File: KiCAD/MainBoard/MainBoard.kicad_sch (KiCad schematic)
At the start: 84 parts, among them J1 DB25, J2 Raspberry_Pi_2_3, P1 CONN_02X04, P10 CONN_01X03, P11 CONN_01X03, P12 CONN_01X03, P13 CONN_01X03, P14 CONN_01X02, P15 CONN_02X07, P16 CONN_02X04, P18 CONN_01X03, P2 CONN_01X04, P3 CONN_02X04, P4 HOLE, P5 HOLE, P6 HOLE, P7 HOLE, P8 CONN_01X02, P9 CONN_01X03, Q1 BSS138, Q2 BSS138, Q3 DMN65D8L, U1 mp2307, U10 SI4425DDY, U11 INA199A2, U12 ADS1015, U13 DYS_mini_ESC, U14 DYS_mini_ESC, U15 DYS_mini_ESC, U2 DYS_mini_ESC, U3 DYS_mini_ESC, U4 DYS_mini_ESC, U5 DYS_mini_ESC, U6 TLV1117LV33, U7 TENDA_P200, U8 pca9685, U9 DYS_mini_ESC

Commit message: moved BLDC to seperate sheet
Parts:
- removed C13, C14, C15, C16, C6, C7, C8, C9: 220uF/25V, Capacitor_SMD:CP_Elec_8x10, symbol Device:C_Polarized_Small
- removed P3: CONN_02X04, Socket_Strips:Socket_Strip_Straight_2x04, symbol MainBoard-rescue:CONN_02X04
- removed U13, U14, U15, U2, U3, U4, U5, U9: DYS_mini_ESC, footprint:DYS_Mini_ESC, symbol custom_lib:DYS_mini_ESC
- P1: value CONN_02X04 -> BDLC Enable; footprint Socket_Strips:Socket_Strip_Straight_2x04 -> Connector_PinSocket_2.54mm:PinSocket_2x08_P2.54mm_Vertical; symbol MainBoard-rescue:CONN_02X04 -> Connector_Generic:Conn_02x08_Odd_Even
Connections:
- net CH10: now also P1.2 (Pin_2)
- net CH11: now also P1.4 (Pin_4)
- net CH12: now also P1.10 (Pin_10); no longer P1.2 (P2)
- net CH13: now also P1.12 (Pin_12); no longer P1.4 (P4)
- net CH14: now also P1.14 (Pin_14); no longer P1.6 (P6)
- net CH15: now also P1.16 (Pin_16); no longer P1.8 (P8)
- net CH6: now also P1.8 (Pin_8)
- net CH7: now also P1.6 (Pin_6)
- net ESC5 renamed Brushless DC Controllers/ESC1
- net ESC6 renamed Brushless DC Controllers/ESC2
- net ESC7 renamed Brushless DC Controllers/ESC3
- net ESC8 renamed Brushless DC Controllers/ESC4
- new net Brushless DC Controllers/ESC5: P1.9 (Pin_9)
- new net Brushless DC Controllers/ESC6: P1.11 (Pin_11)
- new net Brushless DC Controllers/ESC7: P1.13 (Pin_13)
- new net Brushless DC Controllers/ESC8: P1.15 (Pin_15)
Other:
- added sheet Brushless DC Controllers (BLDC.kicad_sch)
- note removed: "BLDC ESC X 8"
- moved on the sheet: C21, D1, D2, P14, Q3, R15, R16, R17, R6, R7, U10, U7

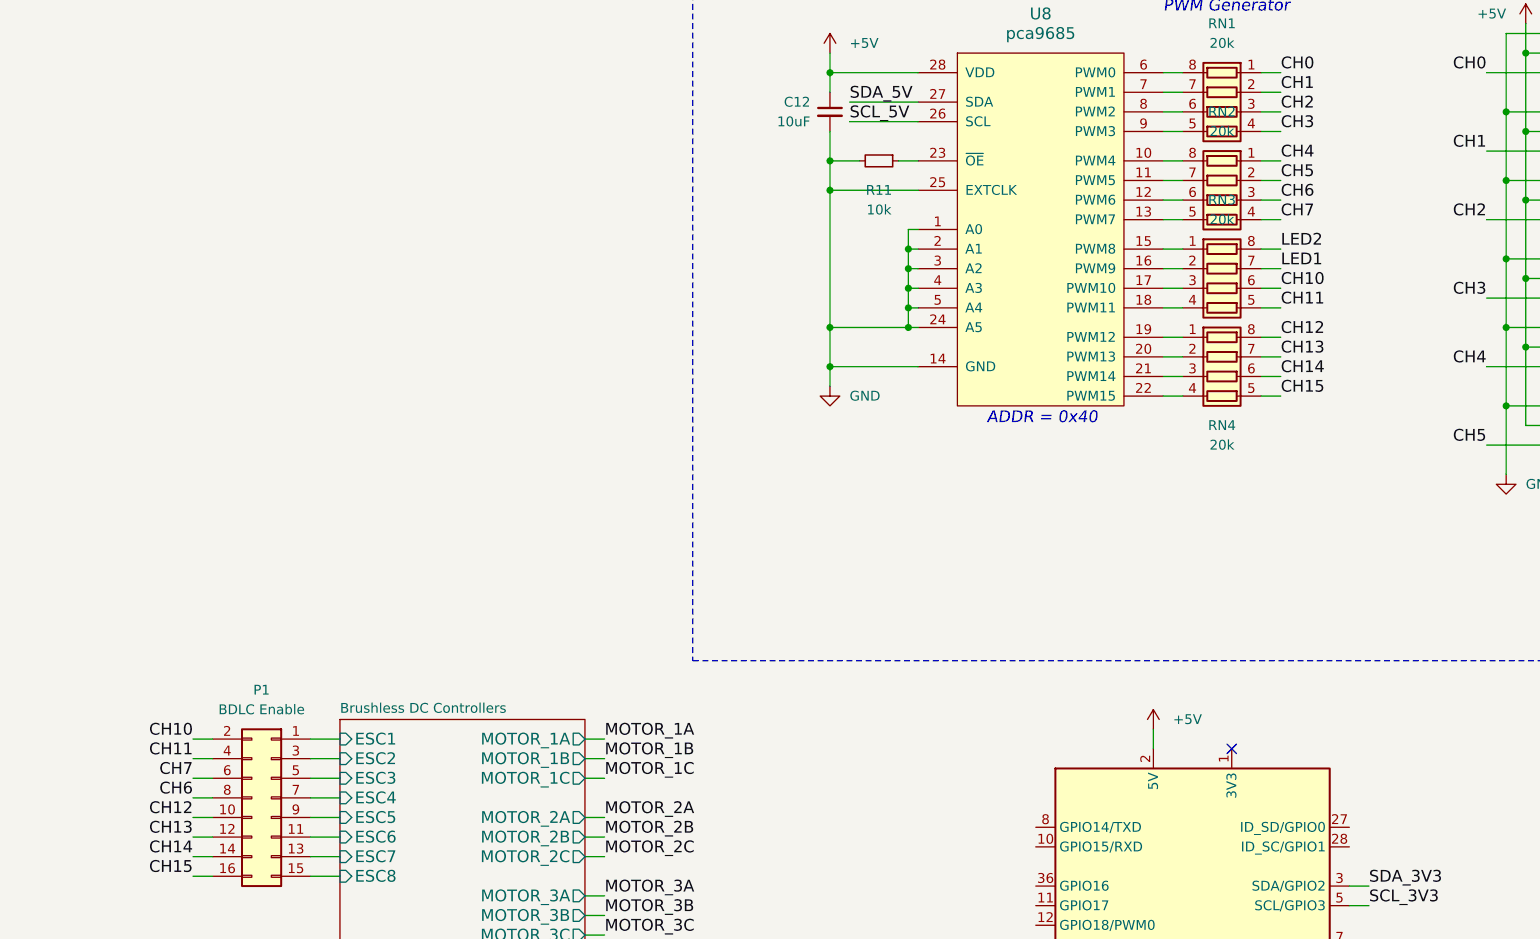
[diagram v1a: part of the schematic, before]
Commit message: change pins
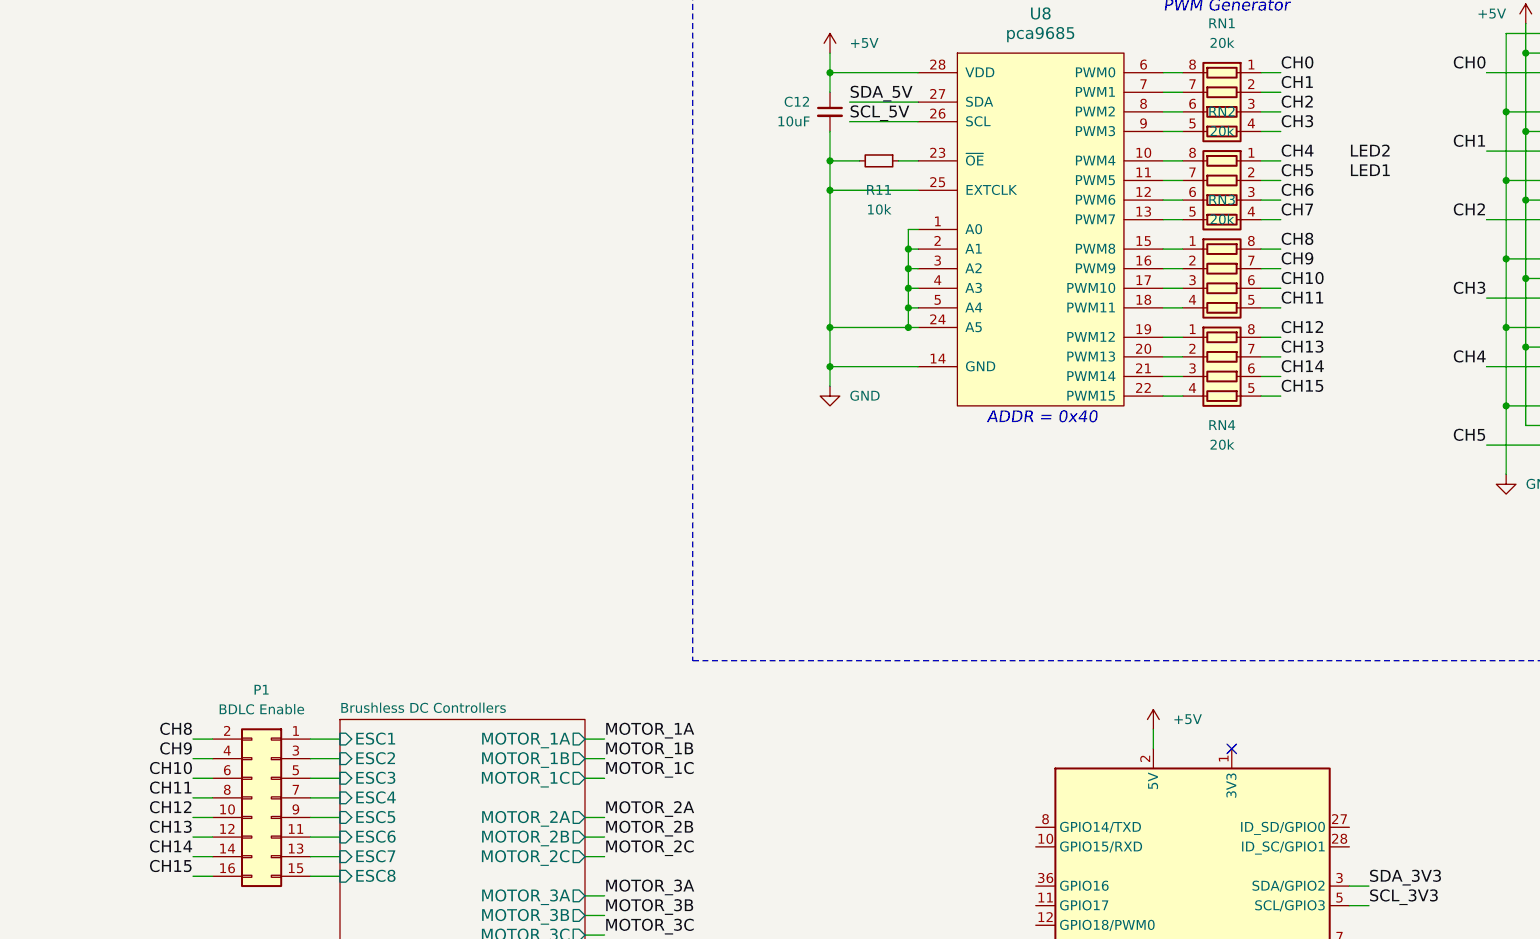
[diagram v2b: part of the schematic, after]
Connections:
- net CH10: now also P1.6 (Pin_6); no longer P1.2 (Pin_2)
- net CH11: now also P1.8 (Pin_8); no longer P1.4 (Pin_4)
- net CH6: no longer P1.8 (Pin_8)
- net CH7: no longer P1.6 (Pin_6)
- net LED1: no longer RN3.7 (R2.2)
- net LED2: no longer RN3.8 (R1.2)
- new net CH8: P1.2 (Pin_2), RN3.8 (R1.2)
- new net CH9: P1.4 (Pin_4), RN3.7 (R2.2)
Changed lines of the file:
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@@
 	)
 	(label "CH11"
-		(at 208.28 113.03 180)
+		(at 208.28 118.11 180)
 		(effects
 			(font
@@
 		)
 	)
-	(label "CH7"
-		(at 208.28 115.57 180)
-		(effects
-			(font
-				(size 1.524 1.524)
-			)
-			(justify right bottom)
-		)
-	)
 	(label "ADC_V"
 		(at 331.47 223.52 0)
@@
 		)
 	)
+	(label "CH9"
+		(at 349.25 49.53 0)
+		(effects
+			(font
+				(size 1.524 1.524)
+			)
+			(justify left bottom)
+		)
+	)
 	(label "LED1"
-		(at 349.25 49.53 0)
+		(at 358.14 38.1 0)
 		(effects
 			(font
@@
 		)
 	)
+	(label "CH8"
+		(at 349.25 46.99 0)
+		(effects
+			(font
+				(size 1.524 1.524)
+			)
+			(justify left bottom)
+		)
+	)
+	(label "CH9"
+		(at 208.28 113.03 180)
+		(effects
+			(font
+				(size 1.524 1.524)
+			)
+			(justify right bottom)
+		)
+	)
 	(label "T+"
 		(at 130.81 246.38 180)
@@
 		)
 	)
+	(label "CH8"
+		(at 208.28 110.49 180)
+		(effects
+			(font
+				(size 1.524 1.524)
+			)
+			(justify right bottom)
+		)
+	)
 	(label "MOTOR_4C"
 		(at 261.62 146.05 0)
@@
 	)
 	(label "LED2"
-		(at 349.25 46.99 0)
+		(at 358.14 35.56 0)
 		(effects
 			(font
@@
 	)
 	(label "CH10"
-		(at 208.28 110.49 180)
+		(at 208.28 115.57 180)
 		(effects
 			(font
@@
 		)
 	)
-	(label "CH6"
-		(at 208.28 118.11 180)
-		(effects
-			(font
-				(size 1.524 1.524)
-			)
-			(justify right bottom)
-		)
-	)
